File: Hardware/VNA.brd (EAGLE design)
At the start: 122 x 98 mm, 588 parts, among them IC1 MIC2253, IC10 MAX2871, IC11 RFSW6042, IC12 RFSW6042, IC13 QPC6324, IC14 RFSA3714, IC15 TRF37A73, IC16 QPC6324, IC17 QPC6324, IC18 QPC6324, IC19 AP2114H, IC2 LM3370SD-4221, IC20 NCP702-3.3, IC21 MAX2871, IC22 LT5560, IC23 THS4521IDGKR, IC24 ADL5801, IC25 NCP702-1.8, IC26 MCP33131D-10-E/MS, IC27 LT5560, IC28 THS4521IDGKR, IC29 ADL5801, IC3 LDL212PU50R, IC30 NCP702-1.8, IC31 MCP33131D-10-E/MS, IC32 THS4521IDGKR, IC33 ADL5801, IC34 NCP702-1.8, IC35 MCP33131D-10-E/MS, IC36 LT5560, IC37 STM32G431CB, IC4 LDL212PU50R, IC5 LDL212PU50R, IC6 LDL212PU50R, IC7 SI5351C, IC8 AP2114H, IC9 NCP702-3.3, J1 PJ-014D, J2 AMPHENOL_132289, J3 AMPHENOL_132289, J4 TYPE-C16P(073), Q1 SSM3J338R, Q2 SSM3J338R, T1 B012-617DB-1-63-B331, T2 B012-617DB-1-63-B331, T3 B012-617DB-1-63-B331, U1 W25Q16BVSN, U2 6SLX9TQG144, X1 SMA_CONNECTOR, X2 SMA_CONNECTOR, Y1 DSB221SDN/26MHz

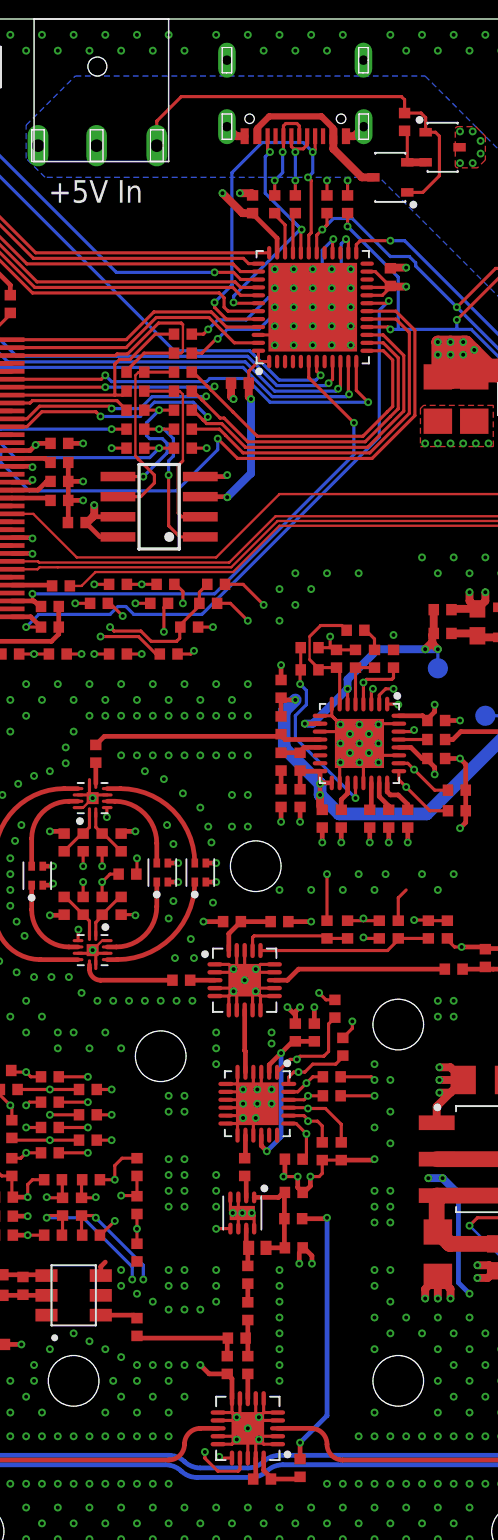
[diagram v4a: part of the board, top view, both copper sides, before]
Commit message: Bugfixes DC jack/amplifier
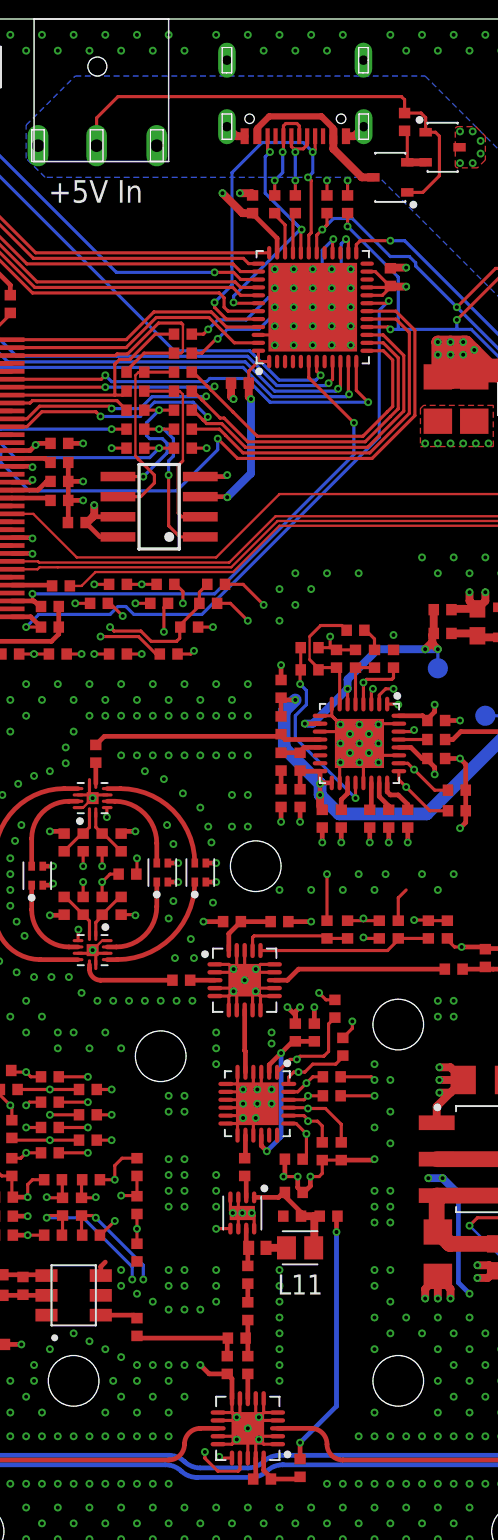
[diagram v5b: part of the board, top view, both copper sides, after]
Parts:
- added L11: 10u, VNA:INDC2012X100N
- moved L23 2.24 mm to (66.1, 20.4)
- moved C73 2.00 mm to (63.8, 20.4), turned to 180 degrees
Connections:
- new net N$270: L11.2, L24.1
- net N$152: now also L11.1; no longer L24.1
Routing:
- net N$168: track 27.1 -> 31.0 mm
- net GND: track 814.5 -> 812.5 mm, vias 1691 -> 1689
- net N$270: track 0.00 -> 1.29 mm
- net N$152: track 6.78 -> 7.32 mm
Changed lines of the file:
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@@
 <drawing>
 <settings>
-<setting alwaysvectorfont="yes"/>
+<setting alwaysvectorfont="no"/>
 <setting verticaltext="up"/>
 </settings>
@@
 <attribute name="VALUE" x="58.895" y="24.135" size="1.27" layer="27" rot="R270"/>
 </element>
-<element name="C73" library="VNA" library_urn="urn:adsk.eagle:library:22367181" package="C0402" package3d_urn="urn:adsk.eagle:package:22367275/2" value="100n" x="63.9" y="18.4" smashed="yes">
-<attribute name="VALUE" x="63.265" y="16.495" size="1.27" layer="27"/>
+<element name="C73" library="VNA" library_urn="urn:adsk.eagle:library:22367181" package="C0402" package3d_urn="urn:adsk.eagle:package:22367275/2" value="100n" x="63.8" y="20.4" smashed="yes" rot="R180">
+<attribute name="VALUE" x="64.435" y="22.305" size="1.27" layer="27" rot="R180"/>
 </element>
 <element name="C72" library="VNA" library_urn="urn:adsk.eagle:library:22367181" package="C0402" package3d_urn="urn:adsk.eagle:package:22367275/2" value="100n" x="63.9" y="21.9" smashed="yes">
@@
 <attribute name="VALUE" x="62.235" y="20.305" size="1.27" layer="27" rot="R180"/>
 </element>
-<element name="L23" library="VNA" library_urn="urn:adsk.eagle:library:22367181" package="R0402" package3d_urn="urn:adsk.eagle:package:22367274/2" value="Ferrite" x="63.87" y="20.24" smashed="yes" rot="R180">
-<attribute name="VALUE" x="64.505" y="22.145" size="1.27" layer="27" rot="R180"/>
+<element name="L23" library="VNA" library_urn="urn:adsk.eagle:library:22367181" package="R0402" package3d_urn="urn:adsk.eagle:package:22367274/2" value="Ferrite" x="66.1" y="20.4" smashed="yes" rot="R180">
+<attribute name="VALUE" x="66.735" y="22.305" size="1.27" layer="27" rot="R180"/>
 </element>
 <element name="L27" library="VNA" library_urn="urn:adsk.eagle:library:22367181" package="R0402" package3d_urn="urn:adsk.eagle:package:22367274/2" value="Ferrite" x="24.8" y="10.5" smashed="yes" rot="R270">
@@
 <attribute name="VALUE" x="103.005" y="36.765" size="1.27" layer="27" rot="R90"/>
 </element>
+<element name="L11" library="VNA" library_urn="urn:adsk.eagle:library:22367181" package="INDC2012X100N" package3d_urn="urn:adsk.eagle:package:26452824/1" value="10u" x="64.3" y="18.4" smashed="yes" rot="R180">
+<attribute name="NAME" x="64.3" y="16.7183" size="1.27" layer="25" rot="R180" align="bottom-center"/>
+<attribute name="VALUE" x="64.3" y="20.0817" size="1.27" layer="27" rot="R180" align="top-center"/>
+</element>
 </elements>
 <signals>
@@
 <via x="61.25" y="20.6" extent="1-16" drill="0.25"/>
 <via x="60.05" y="20.6" extent="1-16" drill="0.25"/>
-<via x="64.25" y="17.4" extent="1-16" drill="0.25"/>
-<via x="65.05" y="17.4" extent="1-16" drill="0.25"/>
 <via x="64.15" y="22.9" extent="1-16" drill="0.25"/>
 <via x="64.95" y="22.9" extent="1-16" drill="0.25"/>
@@
 <wire x1="29.9" y1="23.3" x2="30.4" y2="22.8" width="0.3" layer="1"/>
 <wire x1="30.4" y1="22.8" x2="30.8" y2="22.8" width="0.3" layer="1"/>
-<wire x1="64.25" y1="18.1" x2="64.25" y2="17.4" width="0.3" layer="1"/>
-<wire x1="65.05" y1="17.4" x2="65.05" y2="17.9" width="0.3" layer="1"/>
 <wire x1="64.95" y1="22.9" x2="64.95" y2="22.3" width="0.3" layer="1"/>
 <wire x1="95.5" y1="22.05" x2="95.5" y2="22.65" width="0.3" layer="1"/>
@@
 <wire x1="59.7" y1="10.44" x2="58.56" y2="10.44" width="0.3" layer="1"/>
 <wire x1="58.56" y1="10.44" x2="58" y2="11" width="0.3" layer="1"/>
-<wire x1="65.05" y1="17.9" x2="64.55" y2="18.4" width="0.3" layer="1"/>
-<wire x1="64.55" y1="18.4" x2="64.46" y2="18.4" width="0.3" layer="1"/>
 <wire x1="64.95" y1="22.3" x2="64.55" y2="21.9" width="0.3" layer="1"/>
 <wire x1="64.55" y1="21.9" x2="64.46" y2="21.9" width="0.3" layer="1"/>
@@
 <wire x1="64.3" y1="5.06" x2="64.3" y2="6.1" width="0.3" layer="1"/>
 <via x="64.3" y="6.1" extent="1-16" drill="0.25"/>
-<wire x1="64.3" y1="6.1" x2="66" y2="7.8" width="0.3" layer="16"/>
-<wire x1="66" y1="7.8" x2="66" y2="20.3" width="0.3" layer="16"/>
-<via x="66" y="20.3" extent="1-16" drill="0.25"/>
-<wire x1="66" y1="20.3" x2="65.94" y2="20.24" width="0.3" layer="1"/>
-<wire x1="65.94" y1="20.24" x2="64.43" y2="20.24" width="0.3" layer="1"/>
-<wire x1="66" y1="20.3" x2="66" y2="22.8" width="1" layer="15"/>
+<wire x1="64.3" y1="6.1" x2="66.6" y2="8.4" width="0.3" layer="16"/>
+<wire x1="66.6" y1="8.4" x2="66.6" y2="19.4" width="0.3" layer="16"/>
+<via x="66.6" y="19.4" extent="1-16" drill="0.25"/>
+<wire x1="66.6" y1="19.4" x2="66.6" y2="22.8" width="1" layer="15"/>
 <wire x1="66" y1="22.8" x2="66" y2="32.6" width="1" layer="15"/>
 <wire x1="66" y1="32.6" x2="66" y2="33.3" width="1" layer="15"/>
@@
 <via x="72.4" y="22.8" extent="1-16" drill="0.25"/>
 <wire x1="73.3" y1="22.8" x2="72.4" y2="22.8" width="0.5" layer="15"/>
-<wire x1="72.4" y1="22.8" x2="66" y2="22.8" width="0.5" layer="15"/>
+<wire x1="72.4" y1="22.8" x2="66.6" y2="22.8" width="0.5" layer="15"/>
+<wire x1="66.6" y1="22.8" x2="66" y2="22.8" width="0.5" layer="15"/>
 <via x="75" y="15.5" extent="1-16" drill="0.25"/>
 <wire x1="75" y1="15.5" x2="74.3" y2="16.2" width="0.3" layer="16"/>
@@
 <wire x1="59.7" y1="65.8" x2="61.2" y2="67.3" width="0.5" layer="16"/>
 <wire x1="61.2" y1="67.3" x2="61.2" y2="72" width="0.5" layer="16"/>
+<wire x1="66.6" y1="19.4" x2="66.6" y2="20.34" width="0.3" layer="1"/>
+<wire x1="66.6" y1="20.34" x2="66.66" y2="20.4" width="0.3" layer="1"/>
 </signal>
 <signal name="SCL">
@@
 <signal name="N$152">
 <contactref element="IC15" pad="1"/>
-<contactref element="L24" pad="1"/>
 <contactref element="C72" pad="1"/>
 <contactref element="C73" pad="1"/>
 <contactref element="L23" pad="2"/>
-<wire x1="62.1484" y1="18.4" x2="63.34" y2="18.4" width="0.3" layer="1"/>
 <wire x1="61.4" y1="21.5846" x2="62.9346" y2="21.5846" width="0.3" layer="1"/>
 <wire x1="62.9346" y1="21.5846" x2="63.22" y2="21.87" width="0.3" layer="1"/>
-<wire x1="63.34" y1="18.4" x2="63.31" y2="18.43" width="0.3" layer="1"/>
-<wire x1="63.31" y1="18.43" x2="63.31" y2="20.24" width="0.3" layer="1"/>
-<wire x1="63.31" y1="20.24" x2="63.31" y2="21.78" width="0.3" layer="1"/>
 <wire x1="63.31" y1="21.78" x2="63.22" y2="21.87" width="0.3" layer="1"/>
 <wire x1="63.34" y1="21.9" x2="63.31" y2="21.87" width="0.3" layer="1"/>
 <wire x1="63.31" y1="21.87" x2="63.31" y2="21.78" width="0.3" layer="1"/>
+<contactref element="L11" pad="1"/>
+<wire x1="63.34" y1="21.9" x2="63.34" y2="21.66" width="0.3" layer="1"/>
+<wire x1="64.36" y1="20.64" x2="64.36" y2="20.4" width="0.3" layer="1"/>
+<wire x1="63.34" y1="21.66" x2="64.36" y2="20.64" width="0.3" layer="1"/>
+<wire x1="64.36" y1="20.4" x2="65.2" y2="20.4" width="0.5" layer="1"/>
+<wire x1="65.2" y1="20.4" x2="65.54" y2="20.4" width="0.5" layer="1"/>
+<wire x1="65.1599" y1="18.4" x2="65.2" y2="18.4401" width="0.5" layer="1"/>
+<wire x1="65.2" y1="18.4401" x2="65.2" y2="20.4" width="0.5" layer="1"/>
 </signal>
 <signal name="N$150">
@@
 <contactref element="Q2" pad="1"/>
 <contactref element="R125" pad="1"/>
-<contactref element="J1" pad="3"/>
 <wire x1="72.2296" y1="88.85" x2="72.2296" y2="89.7704" width="0.2" layer="1"/>
 <wire x1="71.0704" y1="85.05" x2="72.05" y2="85.05" width="0.2" layer="1"/>
@@
 <wire x1="70.9" y1="90.06" x2="70.9" y2="90.9" width="0.2" layer="1"/>
 <wire x1="70.9" y1="90.9" x2="70.7" y2="91.1" width="0.2" layer="1"/>
-<wire x1="70.7" y1="91.1" x2="56.8" y2="91.1" width="0.2" layer="1"/>
-<wire x1="55.25" y1="89.55" x2="55.25" y2="88" width="0.2" layer="1"/>
-<wire x1="56.8" y1="91.1" x2="55.25" y2="89.55" width="0.2" layer="1"/>
+<wire x1="70.7" y1="91.1" x2="52.8" y2="91.1" width="0.2" layer="1"/>
+<wire x1="52.8" y1="91.1" x2="51.45" y2="89.75" width="0.2" layer="1"/>
 <wire x1="72.2296" y1="89.7704" x2="71.94" y2="90.06" width="0.2" layer="1"/>
 <wire x1="71.94" y1="90.06" x2="70.9" y2="90.06" width="0.2" layer="1"/>
+<contactref element="J1" pad="3"/>
+<wire x1="51.45" y1="89.75" x2="51.45" y2="88" width="0.2" layer="1"/>
 </signal>
 <signal name="N$312">
@@
 <wire x1="35.26" y1="18.9" x2="35.4" y2="19.04" width="0.3" layer="1"/>
 </signal>
+<signal name="N$270">
+<contactref element="L24" pad="1"/>
+<contactref element="L11" pad="2"/>
+<wire x1="62.1484" y1="18.4" x2="63.4401" y2="18.4" width="0.5" layer="1"/>
+</signal>
 </signals>

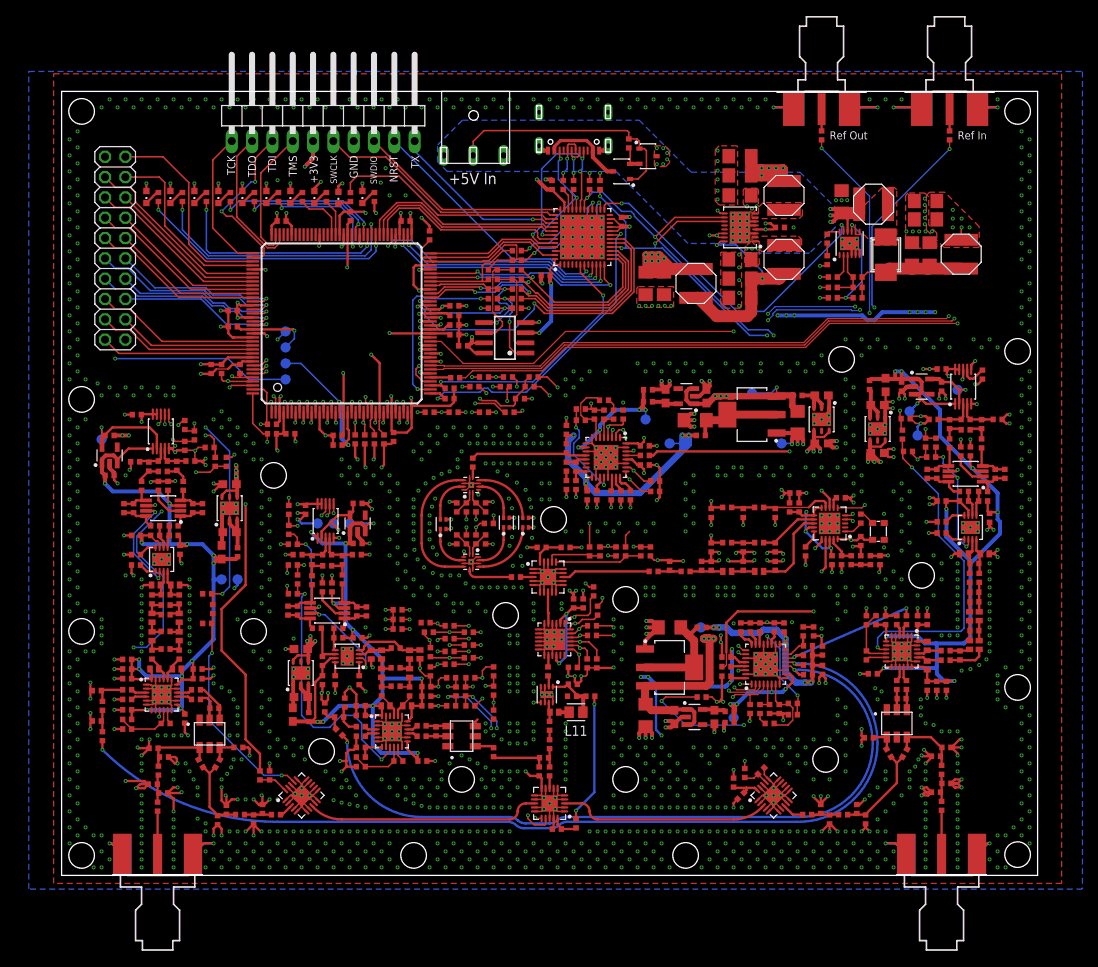
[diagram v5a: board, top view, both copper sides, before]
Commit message: Merged hardware changes from layout_6_layers
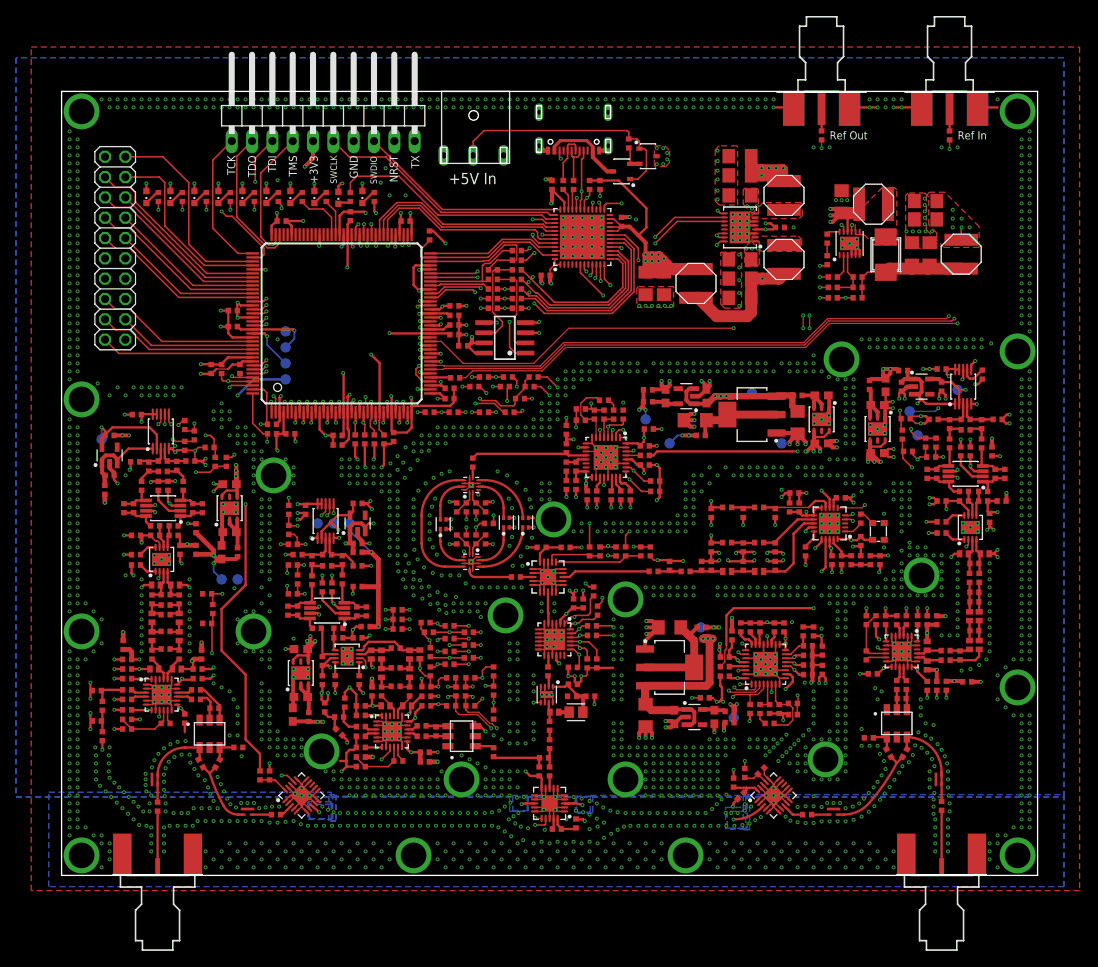
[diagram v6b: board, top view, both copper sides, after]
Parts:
- removed R41, R43, R44, R67, R68, R70, R71: 620, VNA:R0402
- removed R42, R69: 18, VNA:R0402
- removed R51, R52, R74, R75, R78, R79: DNP, VNA:R0402
- removed R77: 0, VNA:R0402
- added L12, L13, L15, L16, L17, L54, L55, L56, L57, L58, L59, L60, L61, L62, L63, L64, L65: Ferrite, VNA:R0402
- J2, J3: value AMPHENOL_132289 -> BU-1420701851; device VNA:AMPHENOL_132289 -> VNA:BU-1420701851
- R40: value 620 -> PAT0816-C-3DB-T5; device VNA:R0402 -> VNA:PAT0816
- R47, R48: device VNA:R0402 -> VNA:PAT0816
- R49: value 0 -> PAT0816-C-3DB-T5; device VNA:R0402 -> VNA:PAT0816
- moved R47 98.3 mm to (109.7, 10.0), turned to 270 degrees
- moved R40 72.5 mm to (96.5, 5.95), turned to 180 degrees
- moved R49 12.3 mm to (23.2, 5.95), turned to 180 degrees
- moved R48 3.03 mm to (11.7, 10.0), turned to 270 degrees
- moved C189 1.40 mm to (37.0, 36.7)
- moved C175 1.14 mm to (45.4, 13.4)
- moved C235 0.41 mm to (80.4, 20.2)
- moved C80 0.20 mm to (82.9, 24.1)
- moved C83 0.20 mm to (82.9, 25.3)
- moved C84 0.20 mm to (82.9, 22.9)
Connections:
- net N$163 renamed +6V
- new net N$271: C99.2, R45.1, R48.1, R48.2, T1.6
- new net N$272: C115.2, IC23.3, L15.1
- new net N$273: C104.1, C105.1, C106.1, C108.1, C111.1, IC24.13, IC24.18, IC24.24, IC24.7, L17.1
- new net N$274: C141.1, C142.1, C143.1, C145.1, C148.1, IC29.13, IC29.18, IC29.24, IC29.7, L54.1
- new net N$275: C156.1, C159.1, L40.1, L41.1, L55.1
- new net N$276: C152.2, IC28.3, L56.1
- new net N$277: C139.2, C140.2, IC27.7, L57.1, R80.1, R81.1
- new net N$278: C166.1, IC30.1, IC30.3, IC31.1, L58.1
- new net N$279: C171.1, C172.1, C175.1, C177.1, C180.1, IC33.13, IC33.18, IC33.24, IC33.7, L59.1
- new net N$280: C190.1, C193.1, L46.1, L47.1, L60.1
- new net N$281: C204.2, C205.2, IC36.7, L61.1, R102.1, R103.1
- new net N$282: C181.2, IC32.3, L62.1
- new net N$283: C195.1, IC34.1, IC34.3, IC35.1, L63.2
- new net N$320: C54.1, C55.1, IC10.28, IC10.32, L64.1
- new net N$322: C83.1, C84.1, IC21.28, IC21.32, L65.1
- net +3V3: now also L64.2, L65.2; no longer C54.1, C55.1, C83.1, C84.1, IC10.28, IC10.32, IC21.28, IC21.32
- net +5V/1: now also L12.2, L13.2, L15.2, L16.2, L17.2; no longer C102.2, C103.2, C104.1, C105.1, C106.1, C108.1, C111.1, C115.2, C119.1, C122.1, C129.1, IC22.7, IC23.3, IC24.13, IC24.18, IC24.24, IC24.7, IC25.1, IC25.3, IC26.1, L32.1, L33.1, R53.1, R54.1
- net +5V/2: now also L54.2, L55.2, L56.2, L57.2, L58.2; no longer C139.2, C140.2, C141.1, C142.1, C143.1, C145.1, C148.1, C152.2, C156.1, C159.1, C166.1, IC27.7, IC28.3, IC29.13, IC29.18, IC29.24, IC29.7, IC30.1, IC30.3, IC31.1, L40.1, L41.1, R80.1, R81.1
- net +5V/3: now also L59.2, L60.2, L61.2, L62.2, L63.1; no longer C171.1, C172.1, C175.1, C177.1, C180.1, C181.2, C190.1, C193.1, C195.1, C204.2, C205.2, IC32.3, IC33.13, IC33.18, IC33.24, IC33.7, IC34.1, IC34.3, IC35.1, IC36.7, L46.1, L47.1, R102.1, R103.1
- net GND: now also R40.3, R47.3, R48.3, R49.3; no longer R40.2, R41.1, R43.1, R44.2, R47.1, R48.2, R51.2, R52.1, R67.2, R68.1, R70.1, R71.2, R74.1, R75.2, R78.2, R79.1
- net N$1: now also R49.1; no longer R40.1, R41.2, R42.2
- net N$2: now also R49.2; no longer R42.1, R43.2, R44.1
- net N$21: now also R40.2; no longer R67.1, R68.2, R69.2
- net N$22: now also R40.1; no longer R69.1, R70.2, R71.1
- net N$236: now also C129.1, IC25.1, IC25.3, IC26.1, L13.1; no longer C99.2, R47.2, R49.1, R51.1
- net N$238: now also C119.1, C122.1, L16.1, L32.1, L33.1; no longer C136.2, R74.2, R77.1, R78.1
- net N$25: now also C102.2, C103.2, IC22.7, L12.1, R53.1, R54.1; no longer R72.1, R75.1, R77.2, R79.2, T2.4
- net N$4: now also C136.2, R47.1, R47.2, R72.1, T2.4; no longer R45.1, R48.1, R49.2, R52.2, T1.6
- net PORT1LO1: now also IC21.12, R32.1; no longer IC21.13, R33.1
- net REFLO1: now also IC21.13, R33.1; no longer IC21.12, R32.1
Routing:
- net +3V3: track 386.3 -> 685.2 mm, vias 69 -> 54
- net GND: track 812.5 -> 666.3 mm, vias 1689 -> 2398
- net +5V/3: track 104.6 -> 57.8 mm, vias 11 -> 7
- net SOURCE_VCC: track 84.8 -> 43.8 mm
- net +5V/4: track 86.2 -> 51.7 mm, vias 7 -> 6
- net +5V/2: track 120.8 -> 87.2 mm, vias 10 -> 8
- net N$279: track 0.00 -> 33.3 mm, vias 0 -> 5
- net +5V/1: track 101.9 -> 71.5 mm, vias 12 -> 6
- net N$274: track 0.00 -> 29.2 mm, vias 0 -> 5
- net N$273: track 0.00 -> 28.6 mm, vias 0 -> 5
- net +6V: track 76.1 -> 51.7 mm
- net HIGHBAND_SELECT: track 46.3 -> 67.8 mm
- net LOWBAND_SELECT: track 49.4 -> 67.4 mm
- net LO1_LD: track 73.7 -> 91.6 mm
- net LO1_RF_EN: track 76.3 -> 94.1 mm
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- added copper zone on layer 14, net +5V
- added copper zone on layer 14, net +5V/4
- added copper zone on layer 14, net GND
- added copper zone on layer 3, net GND
- removed copper zone on layer 15, net +3V3
- removed copper zone on layer 16, net +5V
